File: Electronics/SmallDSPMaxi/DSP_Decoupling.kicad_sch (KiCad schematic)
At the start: 25 parts

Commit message: Finishes SmallDSP Maxi plus the fitting In- and Output Boards
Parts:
- C? (x11): JLC Part Number C307331 -> (none); LCSC Part # (none) -> C307331
- C? (x4): JLC Part Number C96446 -> (none); LCSC Part # (none) -> C96446
- C? (x4): JLC Part Number C52923 -> (none); LCSC Part # (none) -> C52923
- C? (x4): JLC Part Number C15195 -> (none); LCSC Part # (none) -> C15195
- R? (x2): JLC Part Number C25086 -> (none); LCSC Part # (none) -> C25086

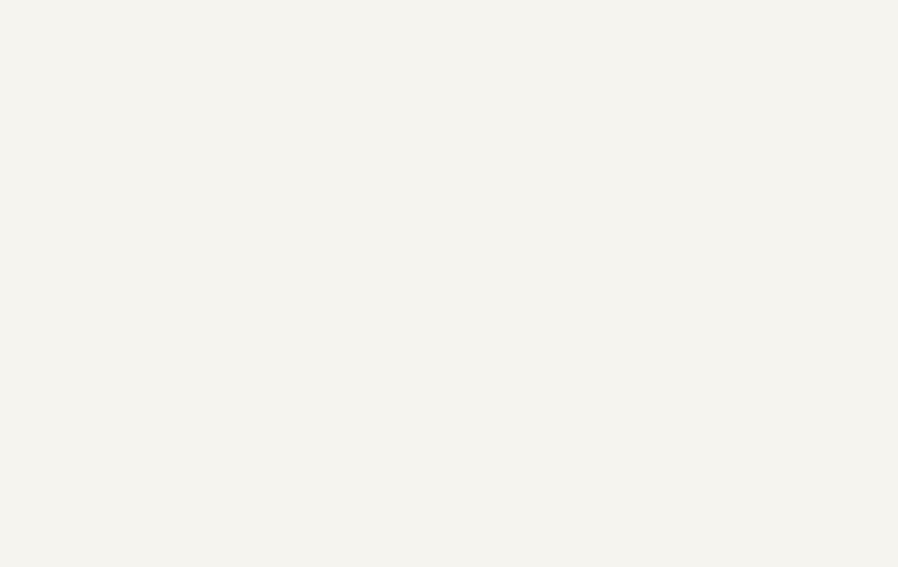
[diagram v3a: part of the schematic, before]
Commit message: Adds clock distributer
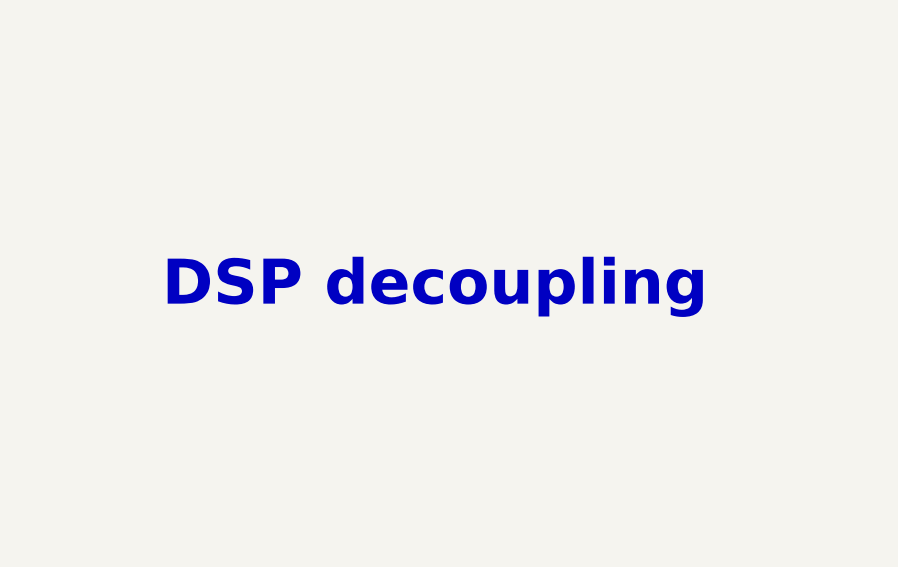
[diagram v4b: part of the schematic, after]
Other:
- note added: "DSP decoupling"
- title: SmallDSP -> SmallDSP Maxi

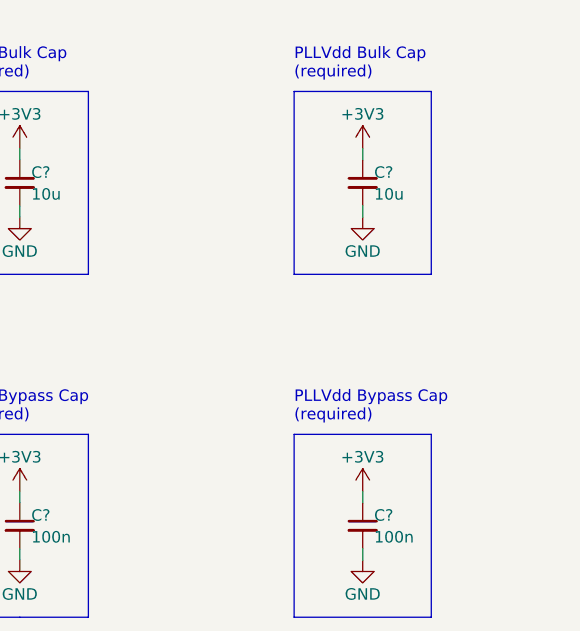
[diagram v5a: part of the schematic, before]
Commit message: adds usb to i2s bridge to micro. Adds tweaks for layout of maxi.
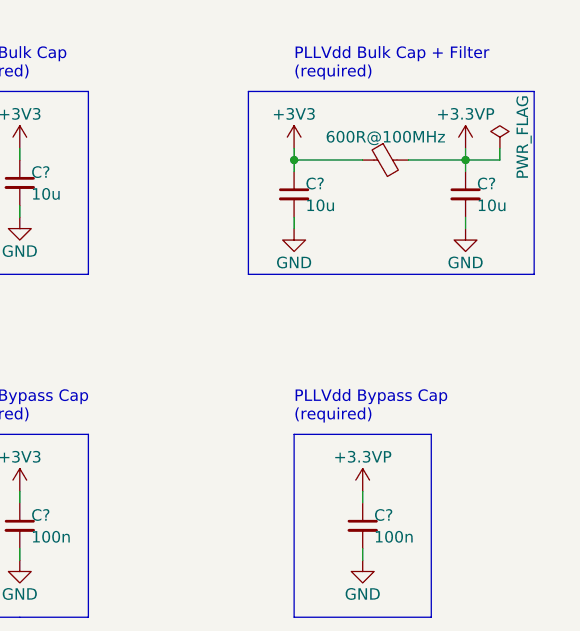
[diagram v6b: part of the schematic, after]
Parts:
- added C?: 10u, Capacitor_SMD:C_0603_1608Metric, symbol Device:C_Small
- added FB?: 600R@100MHz, Inductor_SMD:L_0805_2012Metric, symbol Device:FerriteBead_Small
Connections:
- net +3V3: now also C?.1, FB?.1; no longer C?.1, C?.1
- net GND: now also C?.2
- new net +3.3VP: C?.1, C?.1, FB?.2
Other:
- note added: "PLLVdd Bulk Cap + Filter (required)"
- note removed: "PLLVdd Bulk Cap (required)"
- moved on the sheet: C?
